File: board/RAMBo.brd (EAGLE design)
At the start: 104.1 x 102.9 mm, 252 parts, among them Q1 PSMN7R0-60YS, Q2 PSMN7R0-60YS, Q3 PSMN7R0-60YS, Q4 PSMN7R0-60YS, Q5 PSMN7R0-60YS, T0 PTR1B1,27, T1 PTR1B1,27, T2 PTR1B1,27, T3 PTR1B1,27, U1 ATMEGA32U2-MUR, U2 ATMEGA2560-16AU, U3 TPS54332DDA, U4 AD5206, U5 A4982, U6 A4982, U7 A4982, U8 A4982, U9 A4982, X1 V++2 Out, X10 I2C, X11 MSTBV10, X14 ZMotor, X15 ZMotor, X2 USB B-TH, X21 Z_MIN, X22 Y_MIN, X23 X_MIN, X24 Z_MAX, X25 Y_MAX, X26 X_MAX, X27 T0, X28 T1, X29 T2, X3 T3, X30 V++ Out, X33 MSTBA6, X4 YMotor, X5 PS-ON, X6 E0Motor, X7 E1Motor, X8 XMotor, Y1 16MHz KX-7, Y2 16MHz KX-7

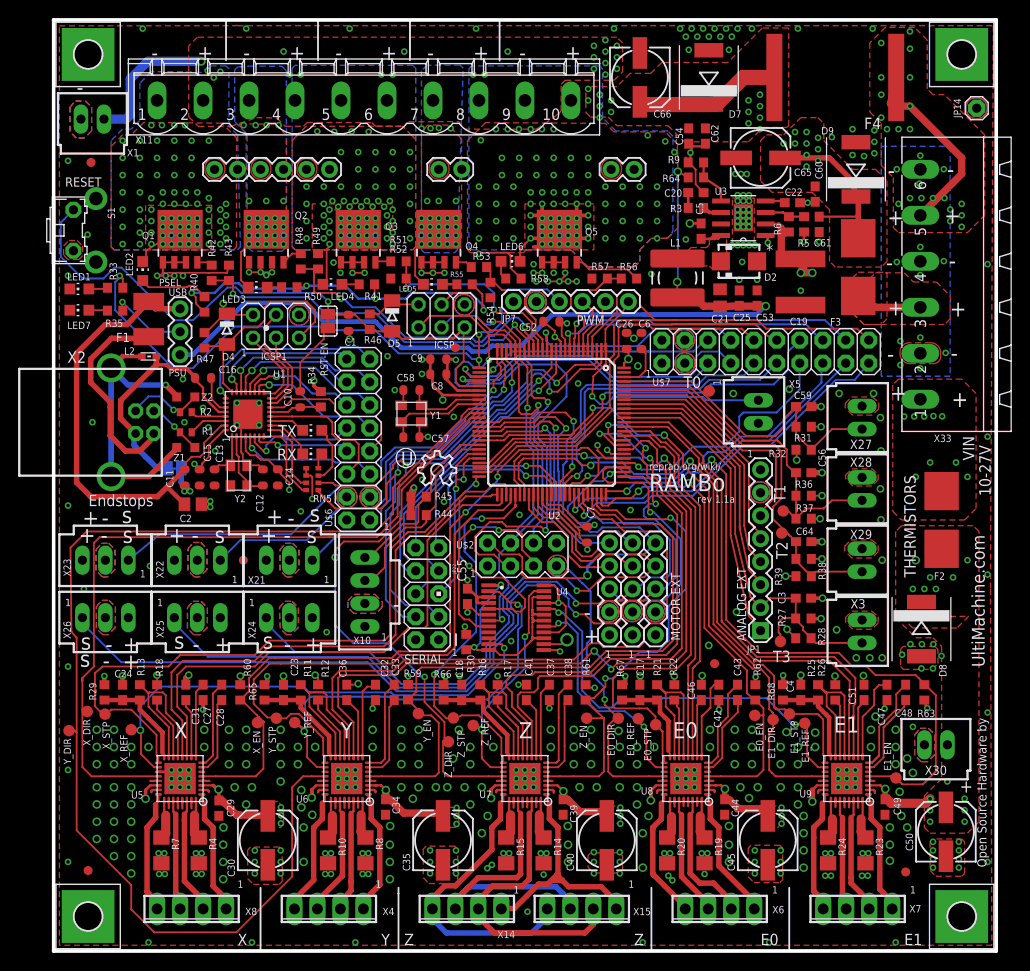
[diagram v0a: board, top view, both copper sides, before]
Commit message: change fan1 mosfet to SOT23, add new fan
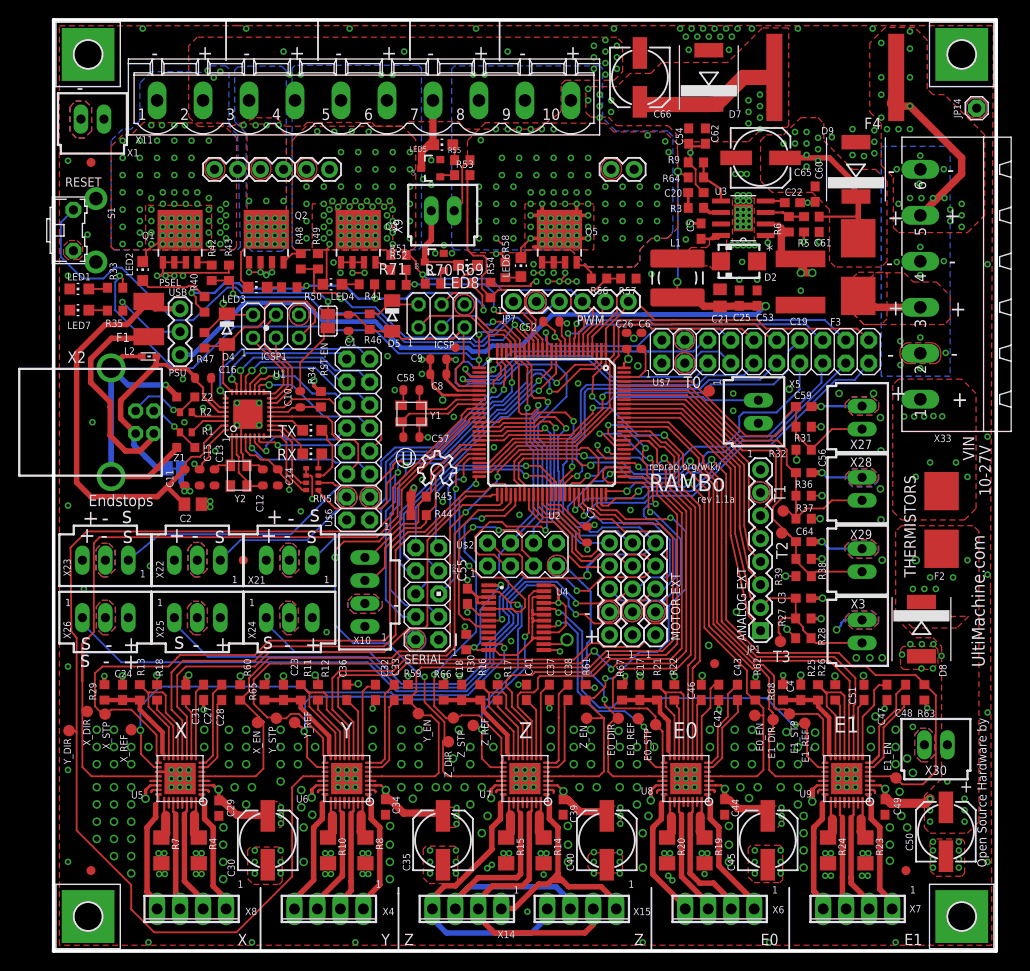
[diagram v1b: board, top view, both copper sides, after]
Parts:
- removed JP15: FIDUCIAL1X2.5, SparkFun:FIDUCIAL-1X2.5
- removed JP19: (no value), SparkFun:1X02
- added JP12: FIDUCIAL1X2, SparkFun:FIDUCIAL-1X2
- added LED8: RED, led:CHIP-LED0805
- added Q8: IRLML6346TRPBF, SparkFun:SOT23-3
- added R69: 1K, resistor:R0603
- added R70: 10r, resistor:R0603
- added R71: 100K, resistor:R0603
- added X9: Fan 2, con-molex:70543-02
- JP8: value FIDUCIAL1X2.5 -> FIDUCIAL1X2; device SparkFun:FIDUCIAL-1X2.5 -> SparkFun:FIDUCIAL-1X2
- Q4: value PSMN7R0-60YS -> IRLML6346TRPBF; device transistor-power:SOT669 -> SparkFun:SOT23-3
- X1: value V++2 Out -> 5V Out
- moved LED5 15.5 mm to (43.1, 89.1)
- moved R55 13.7 mm to (45.1, 87.4)
- moved R53 10.3 mm to (45.1, 85.7)
- moved Q4 7.79 mm to (41.7, 86.5), turned to 90 degrees
- moved R56 3.30 mm to (60.3, 74.3), turned to 180 degrees
- moved R57 3.17 mm to (63.5, 74.3), turned to 0 degrees
- moved LED6 1.31 mm to (51.6, 75.6), turned to 0 degrees
- moved R58 1.30 mm to (49.9, 75.2), turned to 90 degrees
- moved R51 0.95 mm to (38.1, 75.2)
- moved R52 0.70 mm to (38.1, 73.6)
- moved JP2 0.32 mm to (4.13, 8.89)
- moved JP8 0.16 mm to (94.2, 8.89)
- moved C27 0.06 mm to (16.6, 28.6)
- turned R54 to 90 degrees
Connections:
- removed net N$91: Q4.4, R53.2
- removed net PE4: JP7.4, U2.6
- new net FAN-2: JP7.4, R70.1, R71.1, U2.6
- new net N$10: Q4.1, R53.2
- new net N$45: LED8.C, Q8.3, X9.1
- new net N$79: LED8.A, R69.1
- new net N$80: Q8.1, R70.2
- net +12V2: now also R69.2, X9.2; no longer JP19.2, X1.2
- net GND: now also Q8.2, R71.2; no longer Q4.1, Q4.3
- net N$104: now also Q4.3; no longer JP19.1, Q4.MB
- net VCC: now also X1.2
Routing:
- net FAN-2: track 0.00 -> 29.5 mm, vias 0 -> 1
- net GND: track 142.9 -> 158.4 mm, vias 468 -> 473
- net FAN-1: track 13.1 -> 27.0 mm
- net N$45: track 0.00 -> 9.89 mm
- net PE4: track 6.33 -> 0.00 mm
- net N$92: track 7.37 -> 2.76 mm
- net +12V2: track 130.3 -> 126.2 mm, vias 37 -> 36
- net X-DIR: track 85.6 -> 89.4 mm
- net N$104: track 5.11 -> 8.42 mm, vias 27 -> 0
- net N$79: track 0.00 -> 3.16 mm
- net +12V3: track 59.9 -> 56.8 mm
- net L13: track 68.8 -> 65.9 mm
- net N$91: track 1.91 -> 0.00 mm
- net N$10: track 0.00 -> 1.66 mm
- net N$80: track 0.00 -> 1.60 mm
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- removed copper zone on layer 1, net N$104
- removed copper zone on layer 16, net N$104
- removed copper zone on layer 15, net N$45

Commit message: fix reference designator and silk screen
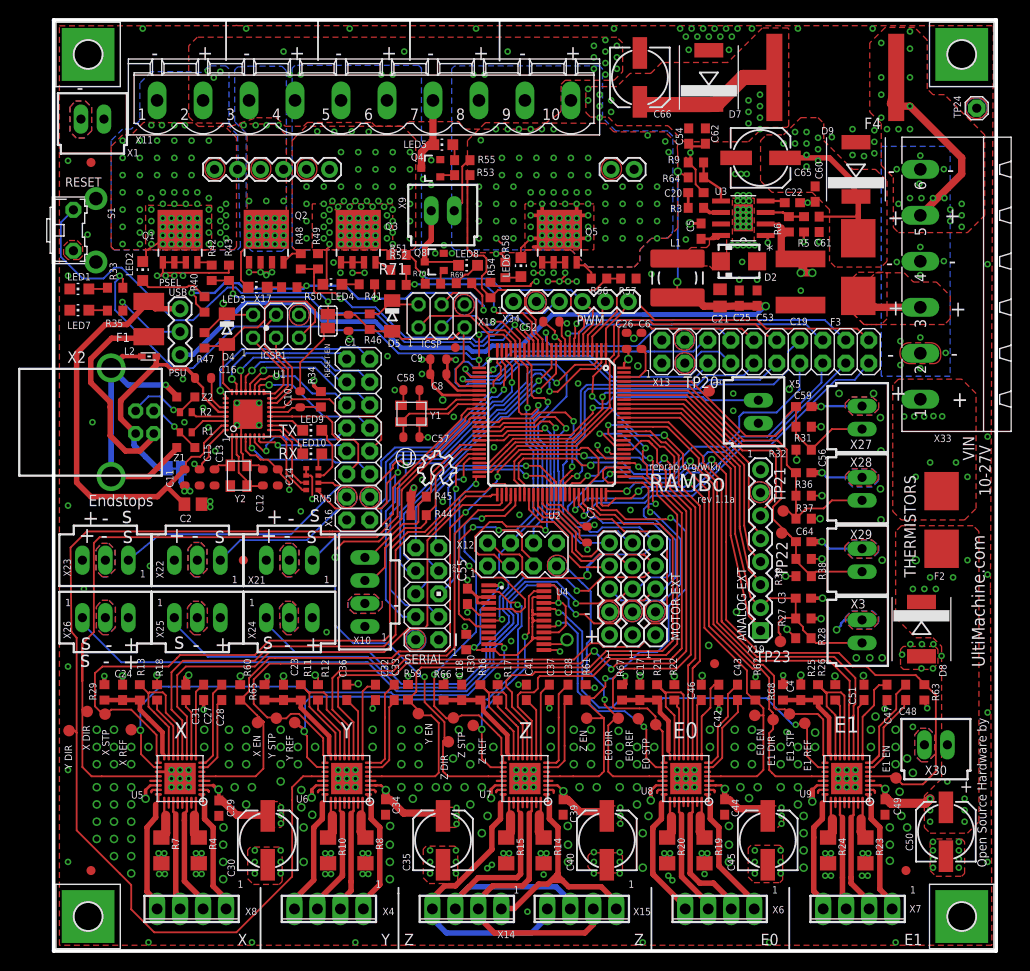
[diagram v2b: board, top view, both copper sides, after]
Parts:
- removed GROUND, RST-EN: (no value), jumper:SJ
- removed JP6: (no value), SparkFun:1X03
- added FID2: FIDUCIAL1X2, SparkFun:FIDUCIAL-1X2
- added X19: Analog-Ext, SparkFun:1X08
- added X20: MX1, SparkFun:1X05
- JP1: value Analog-Ext -> (none); device SparkFun:1X08 -> SparkFun:1X03
- JP2: value FIDUCIAL1X2 -> (none); device SparkFun:FIDUCIAL-1X2 -> jumper:SJ
- JP3: value MX1 -> (none); device SparkFun:1X05 -> jumper:SJ
- moved JP1 71.0 mm to (14.0, 65.9)
- moved JP2 66.1 mm to (30.3, 69.6), turned to 270 degrees
- moved JP3 51.5 mm to (13.3, 53.3), flipped to the bottom, turned to 180 degrees
- renumbered E0_DIR to TP11, E0_EN to TP14, E0_REF to TP12, E0_STP to TP13, E1_DIR to TP15, E1_EN to TP18, E1_REF to TP17, E1_STP to TP16, ICSP to X18, ICSP1 to X17, JP10 to FID3, JP11 to FID5, JP12 to FID1, JP14 to TP24, JP16 to X35, JP17 to X36, JP18 to X37, JP20 to X38, JP22 to X39, JP4 to X31, JP5 to X32, JP7 to X34, JP8 to FID6, JP9 to FID4, RX to LED10, T0 to TP20, T1 to TP21, T2 to TP22, T3 to TP23, TX to LED9, U$2 to X12, U$6 to X16, U$7 to X13, X_DIR to TP1, X_EN to TP4, X_REF to TP3, X_STP to TP2, Y_DIR to TP0, Y_EN to TP7, Y_REF to TP6, Y_STP to TP5, Z_DIR to TP19, Z_EN to TP10, Z_REF to TP9, Z_STP to TP8
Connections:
- net ADC2: now also X19.3; no longer JP1.3
- net ADC3: now also X19.4; no longer JP1.4
- net ADC4: now also X19.5; no longer JP1.5
- net ADC5: now also X19.6; no longer JP1.6
- net GND: now also X19.7, X20.2; no longer GROUND.2, JP1.7
- net N$11: now also JP3.1; no longer GROUND.1
- net PA0: now also X20.3; no longer JP3.3
- net PC5: now also X20.4; no longer JP3.4
- net PK0: now also X19.1; no longer JP1.1
- net PL5: now also X20.5; no longer JP3.5
- net PS_5V: now also JP1.1; no longer JP6.1
- net RESET: now also JP2.1, JP2.2; no longer RST-EN.1, RST-EN.2
- net THERM3: now also X19.2; no longer JP1.2
- net USBVCC: now also JP1.3; no longer JP6.3
- net VCC: now also JP1.2, X19.8, X20.1; no longer JP1.8, JP3.1, JP6.2
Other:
- board text added: "E0 DIR"
- board text added: "E0 EN"
- board text added: "E0 REF"
- board text added: "E0 STP"
- board text added: "E1 DIR"
- board text added: "E1 EN"
- board text added: "E1 REF"
- board text added: "E1 STP"
- board text added: "ICSP"
- board text added: "ICSP1"
- board text added: "RESET-EN"
- board text added: "RX"
- board text added: "TX"
- board text added: "X DIR"
- board text added: "X EN"
- board text added: "X REF"
- board text added: "X STP"
- board text added: "Y DIR"
- board text added: "Y EN"
- board text added: "Y REF"
- board text added: "Y STP"
- board text added: "Z DIR"
- board text added: "Z EN"
- board text added: "Z REF"
- board text added: "Z STP"

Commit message: normalize connector values, fix silk screen
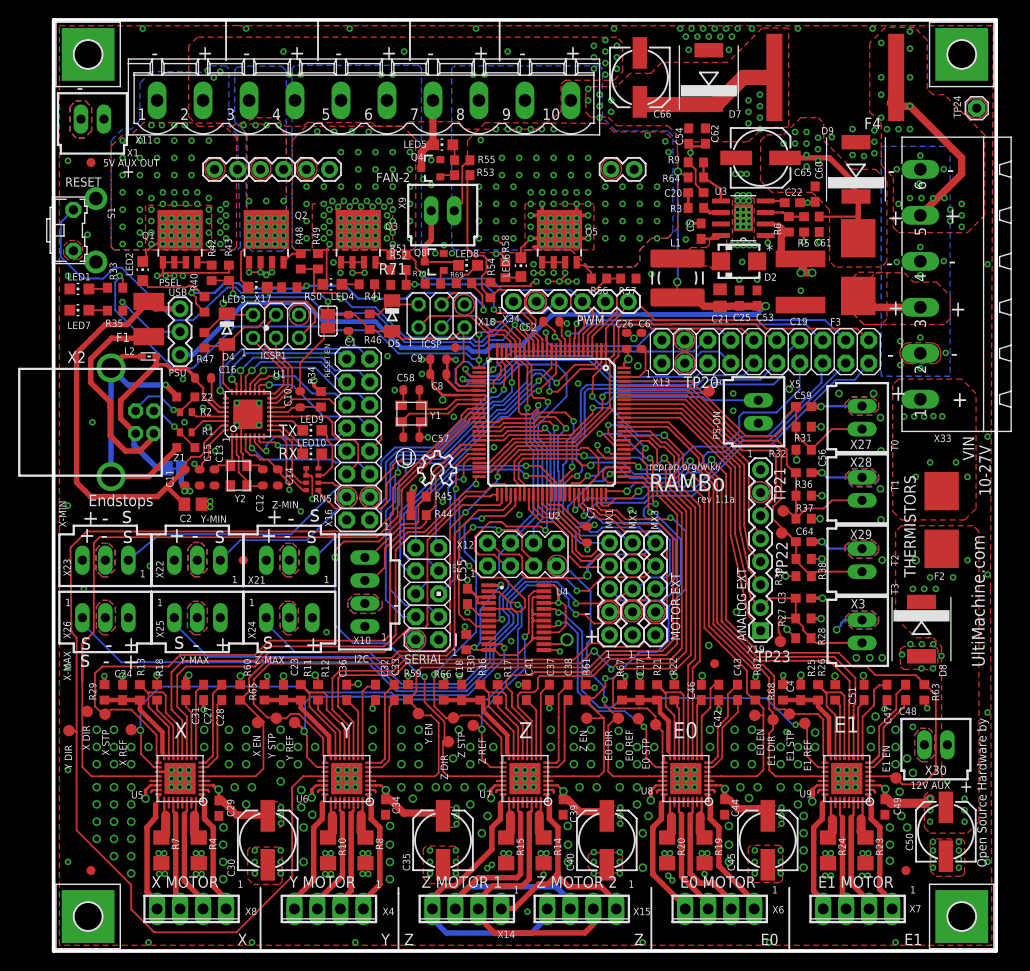
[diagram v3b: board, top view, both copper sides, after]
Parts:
- X1: value 5V Out -> C-GRID-02-70543
- X10: value I2C -> C-GRID-04-70543
- X14, X15: value ZMotor -> C-GRID-04-70543
- X20: value MX1 -> M05PTH
- X21: value Z_MIN -> C-GRID-03-70543
- X22: value Y_MIN -> C-GRID-03-70543
- X23: value X_MIN -> C-GRID-03-70543
- X24: value Z_MAX -> C-GRID-03-70543
- X25: value Y_MAX -> C-GRID-03-70543
- X26: value X_MAX -> C-GRID-03-70543
- X27: value T0 -> C-GRID-02-70543
- X28: value T1 -> C-GRID-02-70543
- X29: value T2 -> C-GRID-02-70543
- X3: value T3 -> C-GRID-02-70543
- X30: value V++ Out -> C-GRID-02-70543
- X31: value MX2 -> M05PTH
- X32: value MX3 -> M05PTH
- X4: value YMotor -> C-GRID-04-70543
- X5: value PS-ON -> C-GRID-02-70543
- X6: value E0Motor -> C-GRID-04-70543
- X7: value E1Motor -> C-GRID-04-70543
- X8: value XMotor -> C-GRID-04-70543
- X9: value Fan 2 -> C-GRID-02-70543
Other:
- board text added: "12V AUX"
- board text added: "5V AUX OUT"
- board text added: "E0 MOTOR"
- board text added: "E1 MOTOR"
- board text added: "FAN-2"
- board text added: "I2C"
- board text added: "MX1"
- board text added: "MX2"
- board text added: "MX3"
- board text added: "PS-ON"
- board text added: "T0"
- board text added: "T1"
- board text added: "T2"
- board text added: "T3"
- board text added: "X MOTOR"
- board text added: "X-MAX"
- board text added: "X-MIN"
- board text added: "Y MOTOR"
- board text added: "Y-MAX"
- board text added: "Y-MIN"
- board text added: "Z MOTOR 1"
- board text added: "Z MOTOR 2"
- board text added: "Z-MAX"
- board text added: "Z-MIN"

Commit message: rev1.1b, move output labels back to _tsilk layer,
remove bstop boxes under mosfets and drivers to reduce chances of
trapped chemicals after wave, add default values for new decoupling caps
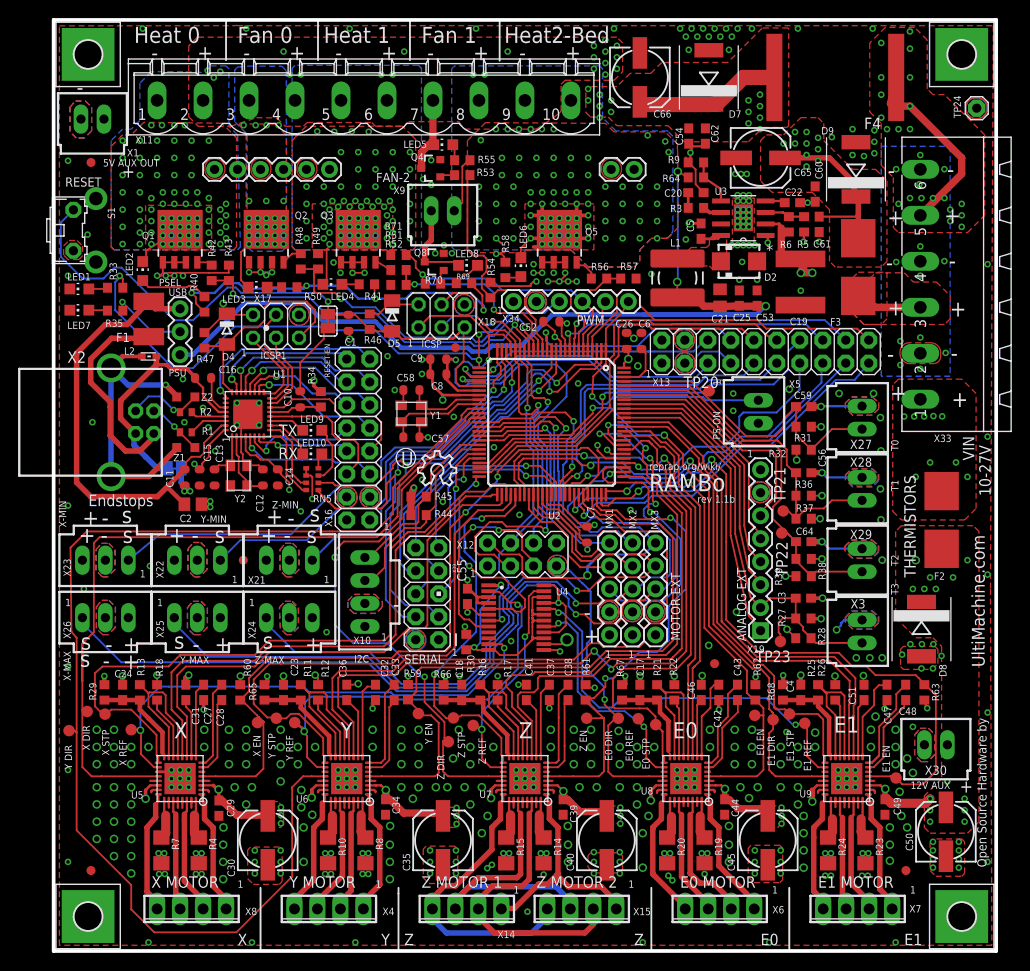
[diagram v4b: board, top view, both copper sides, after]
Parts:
- C25, C61, C62: value . -> 100nF
- C53, C54, C60: value . -> 10nF
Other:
- board text added: "rev 1.1b"
- board text removed: "rev 1.1a"

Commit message: remove stop from JP3, update to eagle6.4
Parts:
- JP3: device jumper:SJ -> ultimachine:SJ-NOSTOP
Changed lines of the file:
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@@
 <?xml version="1.0" encoding="utf-8"?>
 <!DOCTYPE eagle SYSTEM "eagle.dtd">
-<eagle version="6.2">
+<eagle version="6.4">
 <drawing>
 <settings>
@@
 <layer number="45" name="Holes" color="7" fill="1" visible="no" active="yes"/>
 <layer number="46" name="Milling" color="3" fill="1" visible="yes" active="yes"/>
-<layer number="47" name="Measures" color="7" fill="1" visible="yes" active="yes"/>
+<layer number="47" name="Measures" color="7" fill="1" visible="no" active="yes"/>
 <layer number="48" name="Document" color="7" fill="1" visible="yes" active="yes"/>
 <layer number="49" name="Reference" color="7" fill="1" visible="yes" active="yes"/>
@@
 <text x="65.786" y="50.8" size="1.9304" layer="121" ratio="12">RAMBo</text>
 <text x="102.87" y="31.36575" size="1.4224" layer="121" ratio="12" rot="R90">UltiMachine.com</text>
-<dimension x1="0" y1="0" x2="104.14" y2="0" x3="52.07" y3="-19.685" layer="47"/>
-<dimension x1="0" y1="102.87" x2="0" y2="0" x3="-11.43" y3="51.435" layer="47" dtype="vertical"/>
+<dimension x1="0" y1="0" x2="104.14" y2="0" x3="52.07" y3="-19.685" textsize="3.5" layer="47"/>
+<dimension x1="0" y1="102.87" x2="0" y2="0" x3="-11.43" y3="51.435" textsize="3.5" layer="47" dtype="vertical"/>
 <text x="13.3" y="23.5" size="1.778" layer="121">X</text>
 <text x="31.7" y="23.5" size="1.778" layer="121">Y</text>
@@
 <text x="98.708" y="85.5" size="1.778" layer="121" ratio="10">-</text>
 <wire x1="22.86" y1="0" x2="22.86" y2="6.985" width="0.2032" layer="121"/>
-<wire x1="38.1" y1="0" x2="38.1" y2="6.35" width="0.2032" layer="121"/>
-<wire x1="38.1" y1="6.35" x2="38.1" y2="6.985" width="0.2032" layer="121"/>
+<wire x1="38.1" y1="0" x2="38.1" y2="6.985" width="0.2032" layer="121"/>
 <wire x1="66.04" y1="0" x2="66.04" y2="6.985" width="0.2032" layer="121"/>
 <wire x1="81.28" y1="0" x2="81.28" y2="6.985" width="0.2032" layer="121"/>
@@
 <wire x1="49.276" y1="98.3615" x2="49.276" y2="102.8065" width="0.2032" layer="121"/>
 <text x="38.735" y="0.635" size="1.27" layer="121" ratio="10">Z</text>
-<dimension x1="3.81" y1="3.81" x2="100.33" y2="3.81" x3="52.07" y3="-6.985" layer="48"/>
-<dimension x1="3.81" y1="99.06" x2="3.81" y2="3.81" x3="-5.715" y3="51.435" layer="48"/>
-<text x="5.715" y="-4.445" size="1.778" layer="48">H1 3.81,3.81</text>
+<dimension x1="3.81" y1="3.81" x2="100.33" y2="3.81" x3="52.07" y3="-6.985" textsize="3.5" layer="47"/>
+<dimension x1="3.81" y1="99.06" x2="3.81" y2="3.81" x3="-5.715" y3="51.435" textsize="3.5" layer="47"/>
+<text x="5.715" y="-4.445" size="1.778" layer="47">H1 3.81,3.81</text>
 <polygon width="0.2032" layer="41">
 <vertex x="94.3745" y="75.02"/>
@@
 </class>
 </classes>
-<designrules>
+<designrules name="ArduRap4layerExport">
 <description language="en">&lt;b&gt;EAGLE Design Rules&lt;/b&gt;
 &lt;p&gt;
@@
 <param name="psElongationLong" value="100"/>
 <param name="psElongationOffset" value="100"/>
-<param name="mvStopFrame" value="0.2"/>
+<param name="mvStopFrame" value="1"/>
 <param name="mvCreamFrame" value="0.1"/>
-<param name="mlMinStopFrame" value="3mil"/>
+<param name="mlMinStopFrame" value="4mil"/>
 <param name="mlMaxStopFrame" value="4mil"/>
 <param name="mlMinCreamFrame" value="1mil"/>
@@
 <attribute name="NAME" x="16.289" y="60.79" size="0.8128" layer="121"/>
 </element>
-<element name="JP3" library="jumper" package="SJ" value="" x="13.335" y="53.34" smashed="yes" rot="MR180">
-<attribute name="NAME" x="5.969" y="54.737" size="1.27" layer="50" ratio="10" rot="MR180"/>
-<attribute name="VALUE" x="13.7351" y="53.34" size="0.02" layer="28" rot="MR180"/>
-</element>
 <element name="RN5" library="resistor-dil" package="CAY16" value="1k" x="28.575" y="52.1335" smashed="yes" rot="R90">
 <attribute name="NAME" x="28.6635" y="49.5855" size="0.8128" layer="121"/>
@@
 <element name="FID1" library="SparkFun" package="FIDUCIAL-1X2" value="FIDUCIAL1X2" x="4.1275" y="87.122"/>
 <element name="FID6" library="SparkFun" package="FIDUCIAL-1X2" value="FIDUCIAL1X2" x="94.1705" y="8.89"/>
+<element name="JP3" library="ultimachine" package="SJ-NOSTOP" value="" x="13.335" y="53.34" smashed="yes" rot="MR180">
+<attribute name="VALUE" x="13.7351" y="53.34" size="0.02" layer="28" rot="MR180"/>
+</element>
 </elements>
 <signals>
@@
 <contactref element="C15" pad="2"/>
 <contactref element="C11" pad="2"/>
-<contactref element="JP3" pad="2"/>
 <contactref element="C14" pad="2"/>
 <contactref element="U1" pad="33"/>
@@
 <via x="75.08875" y="59.69" extent="1-16" drill="0.381"/>
 <via x="48.65225" y="55.653" extent="1-16" drill="0.381"/>
+<contactref element="JP3" pad="2"/>
 </signal>
 <signal name="VCC">
@@
 <contactref element="U1" pad="28"/>
 <contactref element="C16" pad="2"/>
-<contactref element="JP3" pad="1"/>
 <wire x1="9.06" y1="57.17" x2="7.4025" y2="58.8275" width="0.6096" layer="1"/>
 <wire x1="7.4025" y1="58.8275" x2="7.4025" y2="60.6425" width="0.6096" layer="1"/>
@@
 <wire x1="7.4025" y1="60.6425" x2="7.4025" y2="60.82675" width="0.6096" layer="1"/>
 <wire x1="7.4025" y1="60.82675" x2="11.34575" y2="64.77" width="0.6096" layer="1"/>
+<contactref element="JP3" pad="1"/>
 </signal>
 <signal name="N$18">
